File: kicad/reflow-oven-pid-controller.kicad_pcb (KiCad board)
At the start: 4 copper layers, 42.7 x 74.4 mm, 31 parts, among them J1 1x2P - 5.08mm, J2 1x2P - 5.08mm, J4 1x4P - 2.54mm, J5 1x4P - Right-Angle, J6 1x2P - 5.08mm, Q1 60V - 300mA, Q2 60V - 300mA, U1 3.3v - 500mA, U2 32KB - ARM-M0, U3 1 Channel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

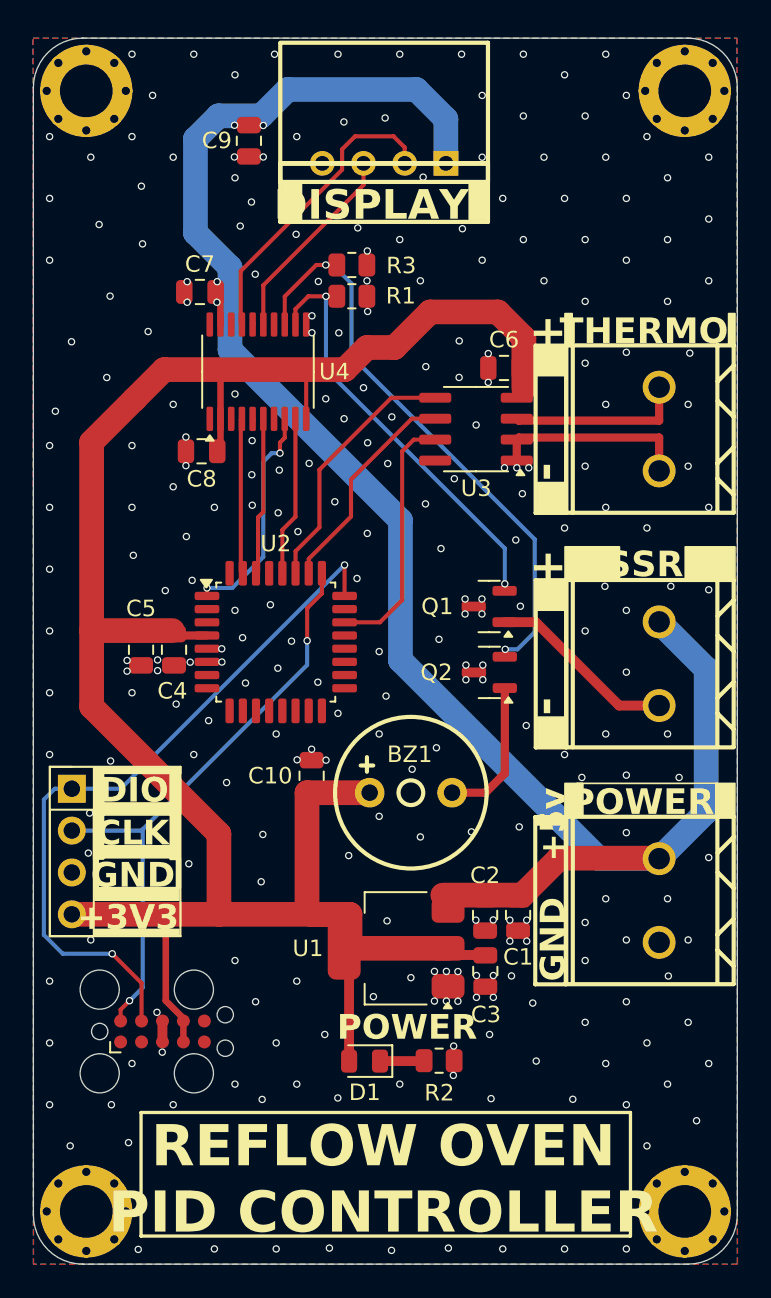
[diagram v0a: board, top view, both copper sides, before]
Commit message: Hardware updates
* Made adjustments for easier hand solder, More spacing and added thermal reliefs
* Changed LDO component  as selected wrong footprint for old one.
* Moved power led to top of board
* Changed power led resistor to hopefully make led less bright
* Added cap to MCU NRST as this was somehow forgotten rendering the MCU none working.
* Adjusted screw terminal footprints slightly as board overhand was too much.
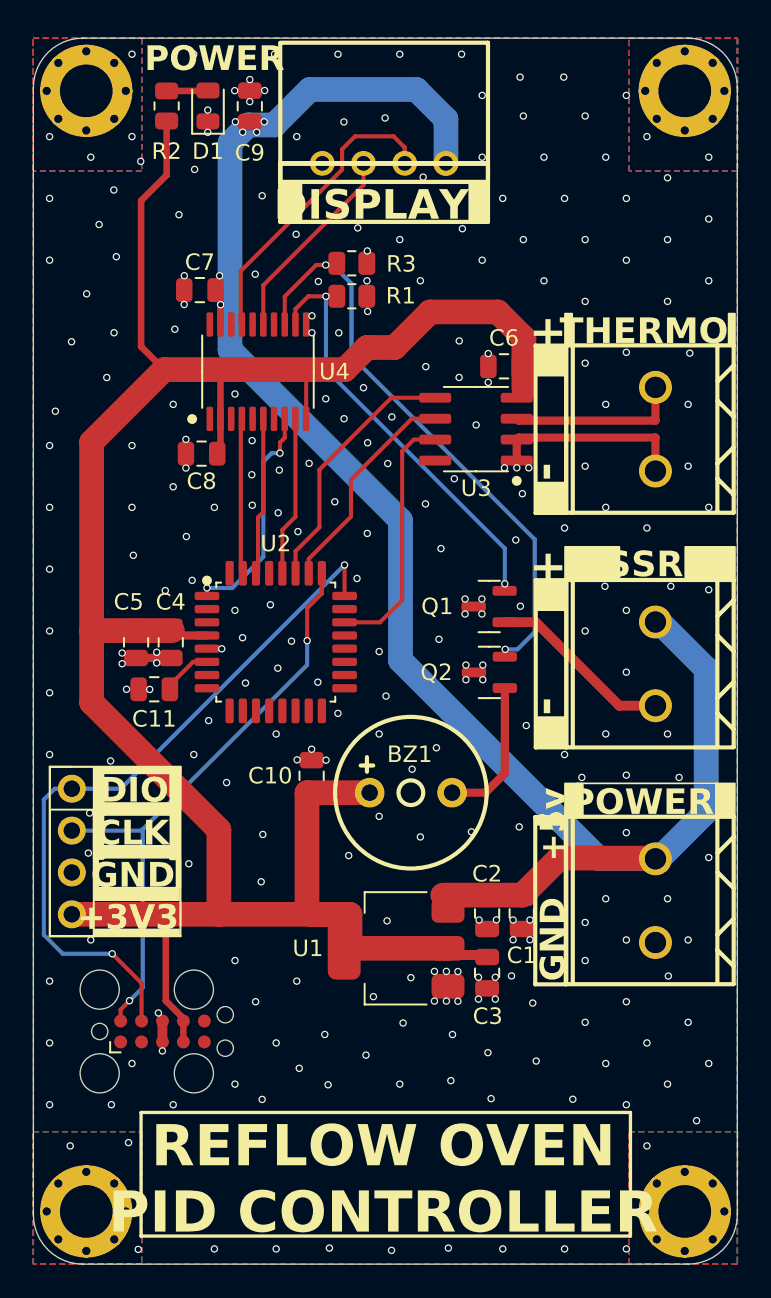
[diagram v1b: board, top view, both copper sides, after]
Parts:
- added C11: 100nF, Capacitor_SMD:C_0805_2012Metric, F.Cu at (131.3, 105.0)
- R2: value 330Ω -> 470Ω
- moved R2 60.3 mm to (132.1, 69.6), turned to -90 degrees
- moved D1 58.7 mm to (134.6, 69.6), turned to 90 degrees
- moved C9 2.10 mm to (137.1, 69.6), turned to 90 degrees
- moved C5 0.54 mm to (130.2, 102.2)
- moved C4 0.49 mm to (132.3, 102.2)
- moved C1 0.24 mm to (153.6, 118.6)
- moved C2 0.15 mm to (151.5, 118.6)
- moved C3 0.15 mm to (151.5, 122.2)
- moved C8 0.14 mm to (134.2, 90.7)
- moved C7 0.11 mm to (134.1, 80.8)
- moved C6 0.10 mm to (152.5, 85.4)
- moved R3 0.10 mm to (143.3, 79.2)
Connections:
- D1 pad 1: Net-(D1-K) -> GND
- D1 pad 2: +3.3V -> Net-(D1-A)
- R2 pad 1: GND -> Net-(D1-A)
- R2 pad 2: Net-(D1-K) -> +3.3V
- U2 pad 6: GND -> Net-(U2-NRST)
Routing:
- net +3.3V: track 138.5 -> 146.4 mm
- net +5V: track 114.4 -> 111.3 mm, vias 4 -> 6
- net Net-(U2-NRST): track 0.00 -> 3.10 mm
- net Net-(D1-K): track 2.69 -> 0.00 mm
- net Net-(D1-A): track 0.00 -> 2.52 mm
- net GND: track 13.3 -> 14.9 mm, vias 270 -> 272
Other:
- board text added: "v1.01"
- board text removed: "v1.00"
